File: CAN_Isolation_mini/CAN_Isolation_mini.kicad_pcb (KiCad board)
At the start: 4 copper layers, 60 x 60 mm, 58 parts, among them J1 S4B-XH-A, J10 Conn_01x04_Pin, J11 Conn_01x04_Pin, J12 Conn_01x04_Pin, J13 Conn_01x04_Pin, J14 Conn_01x04_Pin, J15 Conn_01x04_Pin, J16 Conn_01x04_Pin, J17 Conn_01x04_Pin, J2 Conn_01x04_Pin, J3 Conn_01x04_Pin, J4 Conn_01x04_Pin, J5 Conn_01x04_Pin, J6 Conn_01x04_Pin, J7 Conn_01x04_Pin, J8 Conn_01x04_Pin, J9 Conn_01x04_Pin, U1 MCP2518FDT-H/SL, U2 ISO1042QDWVRQ1, U3 MGS3123R3, U4 MGS1R51205, U5 TVS1800DRVR, U6 DTC114ECAHZGT116, U7 MGS102405, Y1 CSTNE20M0V530000R0

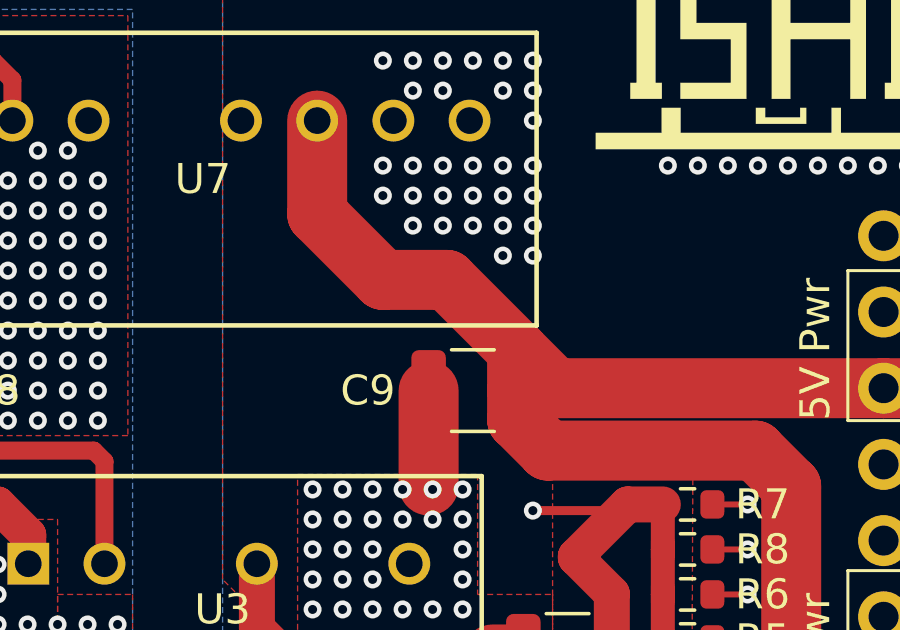
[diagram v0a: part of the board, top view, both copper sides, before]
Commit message: Fix VIA for 5&3.3V line.
Fix VIA for 5&3.3V line.
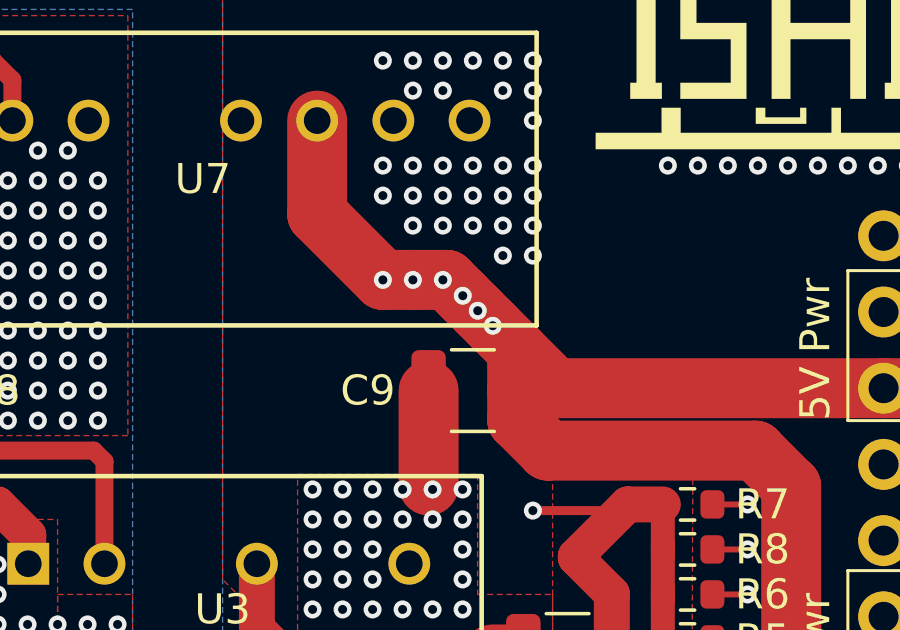
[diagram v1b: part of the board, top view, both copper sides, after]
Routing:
- net +5VP: track 123.0 -> 135.0 mm, vias 0 -> 6
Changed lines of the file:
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@@
 	(segment
 		(start 120.5 80.81)
-		(end 122.635 80.81)
+		(end 121.5 80.81)
 		(width 2)
 		(layer "F.Cu")
@@
 	(segment
 		(start 122.635 80.81)
+		(end 123.1625 81.3375)
+		(width 2)
+		(layer "F.Cu")
+		(net 52)
+	)
+	(segment
+		(start 124.1625 82.3375)
 		(end 124.975 83.15)
+		(width 2)
+		(layer "F.Cu")
+		(net 52)
+	)
+	(segment
+		(start 121.5 80.81)
+		(end 122.5 80.81)
 		(width 2)
 		(layer "F.Cu")
@@
 	)
 	(segment
+		(start 123.6625 81.8375)
+		(end 124.1625 82.3375)
+		(width 2)
+		(layer "F.Cu")
+		(net 52)
+	)
+	(segment
+		(start 122.5 80.81)
+		(end 122.635 80.81)
+		(width 2)
+		(layer "F.Cu")
+		(net 52)
+	)
+	(segment
 		(start 124.975 83.15)
 		(end 126.245 84.42)
@@
 	)
 	(segment
+		(start 123.1625 81.3375)
+		(end 123.6625 81.8375)
+		(width 2)
+		(layer "F.Cu")
+		(net 52)
+	)
+	(segment
 		(start 134.690495 94.58)
 		(end 134.110495 94)
@@
 		(net 52)
 	)
-	(segment
-		(start 123.58 84.42)
-		(end 123.4953 84.42)
-		(width 2)
-		(layer "In1.Cu")
-		(net 52)
-	)
-	(segment
-		(start 123.4953 84.42)
-		(end 118.31 79.2347)
-		(width 2)
-		(layer "In1.Cu")
+	(via
+		(at 122.5 80.81)
+		(size 0.6)
+		(drill 0.3)
+		(layers "F.Cu" "B.Cu")
+		(net 52)
+	)
+	(via
+		(at 124.1625 82.3375)
+		(size 0.6)
+		(drill 0.3)
+		(layers "F.Cu" "B.Cu")
+		(net 52)
+	)
+	(via
+		(at 121.5 80.81)
+		(size 0.6)
+		(drill 0.3)
+		(layers "F.Cu" "B.Cu")
+		(net 52)
+	)
+	(via
+		(at 123.6625 81.8375)
+		(size 0.6)
+		(drill 0.3)
+		(layers "F.Cu" "B.Cu")
+		(net 52)
+	)
+	(via
+		(at 123.1625 81.3375)
+		(size 0.6)
+		(drill 0.3)
+		(layers "F.Cu" "B.Cu")
+		(net 52)
+	)
+	(via
+		(at 120.5 80.81)
+		(size 0.6)
+		(drill 0.3)
+		(layers "F.Cu" "B.Cu")
 		(net 52)
 	)
@@
 	)
 	(segment
+		(start 121.39 80.81)
+		(end 125 84.42)
+		(width 2)
+		(layer "In1.Cu")
+		(net 52)
+	)
+	(segment
+		(start 118.31 79.02235)
+		(end 118.31 75.5)
+		(width 2)
+		(layer "In1.Cu")
+		(net 52)
+	)
+	(segment
+		(start 122.39 80.81)
+		(end 126 84.42)
+		(width 2)
+		(layer "In1.Cu")
+		(net 52)
+	)
+	(segment
 		(start 144.81 94.58)
 		(end 135.08 94.58)
@@
 	)
 	(segment
+		(start 126 84.42)
+		(end 125 84.42)
+		(width 2)
+		(layer "In1.Cu")
+		(net 52)
+	)
+	(segment
+		(start 125 84.42)
+		(end 123.58 84.42)
+		(width 2)
+		(layer "In1.Cu")
+		(net 52)
+	)
+	(segment
 		(start 144.81 84.42)
-		(end 123.58 84.42)
+		(end 126 84.42)
 		(width 2)
 		(layer "In1.Cu")
@@
 	)
 	(segment
+		(start 121.39 80.81)
+		(end 122.39 80.81)
+		(width 2)
+		(layer "In1.Cu")
+		(net 52)
+	)
+	(segment
+		(start 123.58 84.42)
+		(end 123.58 84.29235)
+		(width 2)
+		(layer "In1.Cu")
+		(net 52)
+	)
+	(segment
+		(start 120.5 80.81)
+		(end 121.39 80.81)
+		(width 2)
+		(layer "In1.Cu")
+		(net 52)
+	)
+	(segment
 		(start 125.66 86.5)
 		(end 123.58 84.42)
@@
 	)
 	(segment
-		(start 118.31 79.2347)
-		(end 118.31 75.5)
-		(width 2)
-		(layer "In1.Cu")
-		(net 52)
-	)
-	(segment
 		(start 133 86.5)
 		(end 125.66 86.5)
 		(width 2)
 		(layer "In1.Cu")
+		(net 52)
+	)
+	(segment
+		(start 123.58 84.29235)
+		(end 118.31 79.02235)
+		(width 2)
+		(layer "In1.Cu")
